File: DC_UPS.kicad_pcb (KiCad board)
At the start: 2 copper layers, 126.2 x 68.6 mm, 31 parts, among them J1 USB_B_Micro, J2 POWER, J3 STATUS, Q1 SIS402DN, Q2 SIS402DN, U1 LTC4040

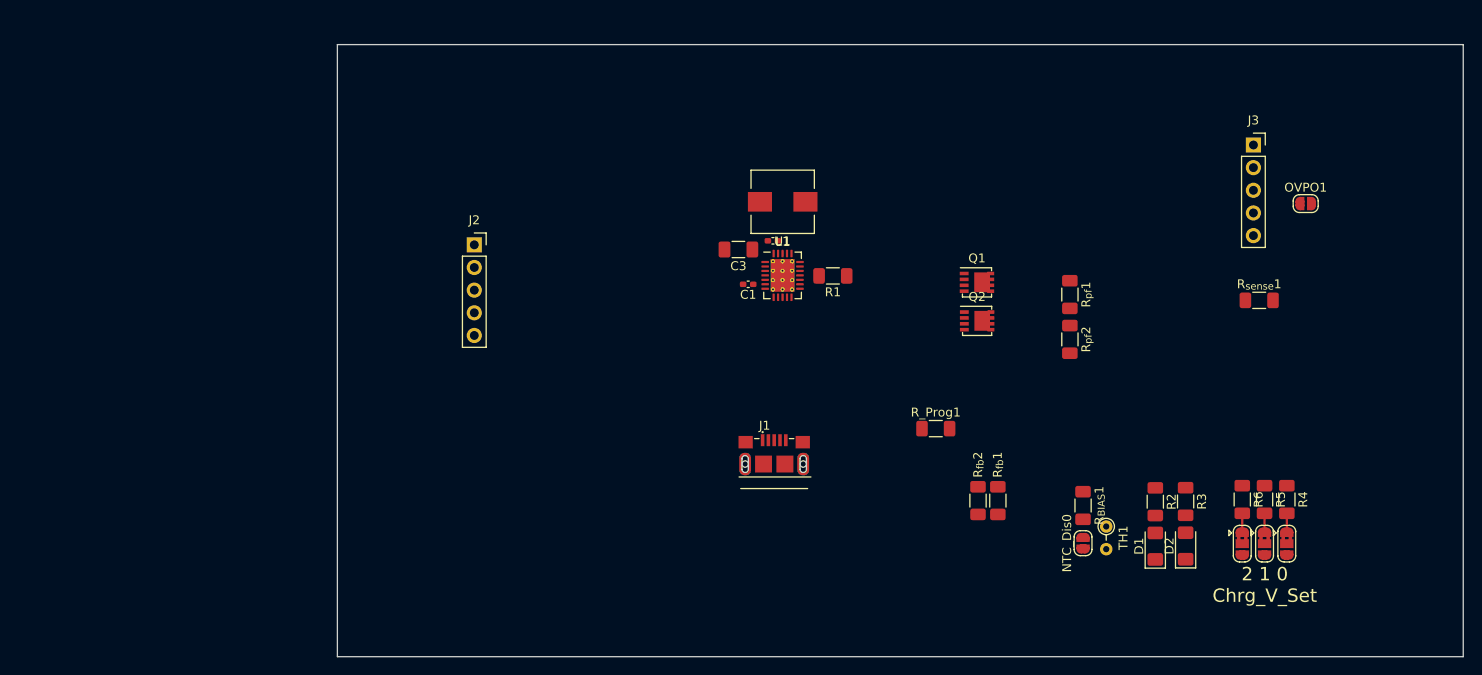
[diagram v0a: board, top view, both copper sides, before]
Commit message: [Board]Build board without connectors
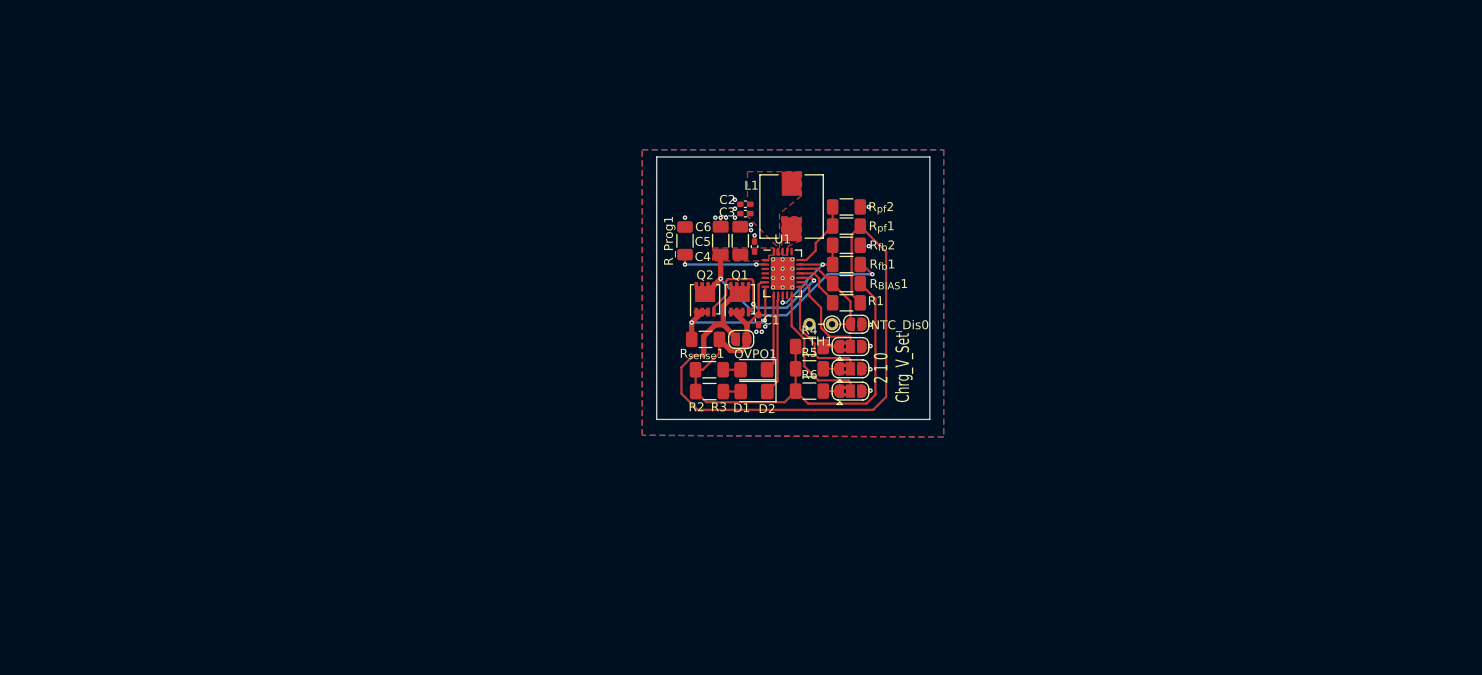
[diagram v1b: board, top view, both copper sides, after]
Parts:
- removed J1: USB_B_Micro, DC_UPS-backups:TE_2013499-1
- removed J2: POWER, Connector_PinSocket_2.54mm:PinSocket_1x05_P2.54mm_Vertical
- removed J3: STATUS, Connector_PinSocket_2.54mm:PinSocket_1x05_P2.54mm_Vertical
- added C3: 0,1uF, Capacitor_SMD:C_0402_1005Metric_Pad0.74x0.62mm_HandSolder, F.Cu at (109.6, 49.1)
- added C4: 0,1uF, Capacitor_SMD:C_0402_1005Metric_Pad0.74x0.62mm_HandSolder, F.Cu at (110.6, 52.9)
- added C6: 100u, Capacitor_SMD:C_1206_3216Metric_Pad1.33x1.80mm_HandSolder, F.Cu at (106.8, 52.2)
- moved OVPO1 65.1 mm to (109.1, 63.2)
- moved R_{sense}1 62.2 mm to (105.1, 63.2), turned to 180 degrees
- moved R4 56.2 mm to (116.8, 64.0), turned to 0 degrees
- moved R3 55.4 mm to (105.5, 66.7), turned to 0 degrees
- moved F_SEL0 53.7 mm to (121.3, 64.0), turned to 0 degrees
- moved R5 53.1 mm to (116.8, 66.5), turned to 0 degrees
- moved D2 52.3 mm to (110.5, 66.7), turned to 180 degrees
- moved R2 51.5 mm to (105.5, 69.1), turned to 0 degrees
- moved F_SEL1 50.4 mm to (121.3, 66.5), turned to 0 degrees
- moved R6 50.0 mm to (116.8, 69.0), turned to 0 degrees
- moved D1 48.2 mm to (110.5, 69.1), turned to 180 degrees
- moved F_SEL2 47.1 mm to (121.3, 69.0), turned to 0 degrees
- moved TH1 38.2 mm to (119.3, 61.5), turned to 180 degrees
- moved R_{BIAS}1 36.4 mm to (120.9, 57.0), turned to 180 degrees
- moved NTC_Dis0 35.3 mm to (122.0, 61.5), turned to 180 degrees
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- renumbered C3 to C5
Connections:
- R4 pad 1: /V_SYS -> /Vin
- R5 pad 1: /V_SYS -> /Vin
- R6 pad 1: /V_SYS -> /Vin
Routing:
- net /Input_V: track 0.00 -> 71.6 mm
- net /Vin: track 0.00 -> 62.9 mm
- net /V_SYS: track 0.00 -> 27.6 mm, vias 0 -> 2
- net /I_GATE: track 0.00 -> 20.9 mm, vias 0 -> 2
- net /CLN: track 0.00 -> 16.9 mm, vias 0 -> 2
- net /F2: track 0.00 -> 15.5 mm
- net /F1: track 0.00 -> 13.5 mm
- net /BSTFB: track 0.00 -> 13.0 mm, vias 0 -> 2
- net /NTC: track 0.00 -> 11.8 mm
- net /~{FAULT}: track 0.00 -> 11.3 mm
- net /F0: track 0.00 -> 11.1 mm
- net /CHRG_PROG: track 0.00 -> 10.0 mm, vias 0 -> 2
- net /~{CHRG}: track 0.00 -> 8.66 mm
- net /POWER_SENSE: track 0.00 -> 8.02 mm
- net Net-(R1-Pad2): track 0.00 -> 5.73 mm
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- added copper zone on F.Cu, net /BAT_+
- added copper zone on F.Cu, net /V_SYS
- added copper zone on B.Cu, net GND
- added copper zone on F.Cu, net GND
- added copper zone on F.Cu, net Net-(L1-Pad1)
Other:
- board size 126.2 x 68.6 mm -> 30.6 x 29.4 mm

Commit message: [Board]Finish product rev 1
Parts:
- removed TH1: NTC, Resistor_THT:R_Axial_DIN0204_L3.6mm_D1.6mm_P2.54mm_Vertical
- added J2: POWER, Castellated_Header:CastellatedPinHeader_2.54mm_5, F.Cu at (31.5, 50.1)
- added J3: STATUS, Castellated_Header:CastellatedPinHeader_2.54mm_5, B.Cu at (58.5, 50.1)
- added J4: BAT_CONN, Connector_JST:JST_SH_BM03B-SRSS-TB_1x03-1MP_P1.00mm_Vertical, F.Cu at (57.8, 33.3)
- added kibuzzard-63A19CFD: G***, kibuzzard-63A19CFD, F.Cu at (54.7, 51.2)
- added kibuzzard-63A19D17: G***, kibuzzard-63A19D17, F.Cu at (54.7, 53.8)
- added kibuzzard-63A19D4B: G***, kibuzzard-63A19D4B, F.Cu at (54.7, 56.2)
- added kibuzzard-63A19E71: G***, kibuzzard-63A19E71, F.Cu at (56.5, 53.8)
- added kibuzzard-63A19F8A: G***, kibuzzard-63A19F8A, F.Cu at (42.5, 50.4)
- added kibuzzard-63A19F98: G***, kibuzzard-63A19F98, F.Cu at (48.5, 48.7)
- added kibuzzard-63A1A047: G***, kibuzzard-63A1A047, F.Cu at (58.3, 37.3)
- added kibuzzard-63A1A128: G***, kibuzzard-63A1A128, F.Cu at (54.6, 33.2)
- added kibuzzard-63A1A287: G***, kibuzzard-63A1A287, F.Cu at (43.3, 58.5)
- added kibuzzard-63A1A2AA: G***, kibuzzard-63A1A2AA, F.Cu at (36.8, 58.5)
- added kibuzzard-63A1A4C9: G***, kibuzzard-63A1A4C9, B.Cu at (35.7, 50.1)
- added kibuzzard-63A1A50F: G***, kibuzzard-63A1A50F, B.Cu at (35.0, 47.5)
- added kibuzzard-63A1A543: G***, kibuzzard-63A1A543, B.Cu at (35.3, 45.0)
- added kibuzzard-63A1A568: G***, kibuzzard-63A1A568, B.Cu at (34.2, 40.0)
- added kibuzzard-63A1A568: G***, kibuzzard-63A1A568, B.Cu at (34.2, 42.5)
- added kibuzzard-63A1A71E: G***, kibuzzard-63A1A71E, B.Cu at (54.3, 42.5)
- added kibuzzard-63A1A72A: G***, kibuzzard-63A1A72A, B.Cu at (53.5, 45.0)
- added kibuzzard-63A1A734: G***, kibuzzard-63A1A734, B.Cu at (54.7, 47.5)
- added kibuzzard-63A1A785: G***, kibuzzard-63A1A785, B.Cu at (55.1, 50.1)
- added kibuzzard-63A1A798: G***, kibuzzard-63A1A798, B.Cu at (53.1, 39.9)
- moved R2 72.5 mm to (34.5, 55.1), turned to -90 degrees
- moved D2 72.4 mm to (39.0, 55.1), turned to -90 degrees
- moved C1 71.2 mm to (41.0, 48.3)
- moved C2 71.2 mm to (39.6, 35.3)
- moved C3 71.2 mm to (39.6, 36.4)
- moved C4 71.2 mm to (40.6, 40.0)
- moved C5 71.2 mm to (39.0, 39.4)
- moved C6 71.2 mm to (36.8, 39.4)
- moved F_SEL0 71.2 mm to (51.4, 51.2)
- moved F_SEL1 71.2 mm to (51.4, 53.8)
- moved F_SEL2 71.2 mm to (51.4, 56.2)
- moved L1 71.2 mm to (44.8, 35.5)
- moved NTC_Dis0 71.2 mm to (52.0, 48.8)
- moved OVPO1 71.2 mm to (39.1, 50.5)
- moved Q1 71.2 mm to (38.9, 46.0)
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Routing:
- net /CLPROG: track 0.00 -> 20.9 mm, vias 0 -> 1
- net /~{CHRG}: track 8.66 -> 27.2 mm, vias 0 -> 1
- net /~{RST_OUT}: track 0.00 -> 16.5 mm, vias 0 -> 1
- net /NTC: track 11.8 -> 27.8 mm
- net /~{POWER_FAIL}: track 0.00 -> 14.3 mm, vias 0 -> 1
- net /~{FAULT}: track 11.3 -> 24.6 mm, vias 0 -> 1
- net /BAT_+: track 0.00 -> 12.6 mm
- net /CHRG_PROG: track 10.0 -> 17.7 mm
- net Net-(D1-Pad2): track 1.95 -> 8.31 mm
- net /Vin: track 62.9 -> 66.7 mm
- net /V_SYS: track 27.6 -> 31.3 mm
- net /Input_V: track 71.6 -> 75.0 mm
- net /CLN: track 16.9 -> 19.6 mm
- net /BSTFB: track 13.0 -> 14.7 mm
- net /F0: track 11.1 -> 9.82 mm
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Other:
- board size 30.6 x 29.4 mm -> 30 x 30 mm

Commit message: [Board][Readme]Update
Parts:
- C3: renamed from C2; footprint Capacitor_SMD:C_0402_1005Metric_Pad0.74x0.62mm_HandSolder -> Capacitor_SMD:C_0805_2012Metric_Pad1.18x1.45mm_HandSolder
- moved C3 0.68 mm to (39.1, 34.8)
- renumbered C3 to C2
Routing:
- net /V_SYS: track 31.3 -> 26.8 mm
- net GND: vias 23 -> 25
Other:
- board text removed: "2 1 0 Chrg_V_Set"
